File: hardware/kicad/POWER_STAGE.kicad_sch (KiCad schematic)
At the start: 0 parts

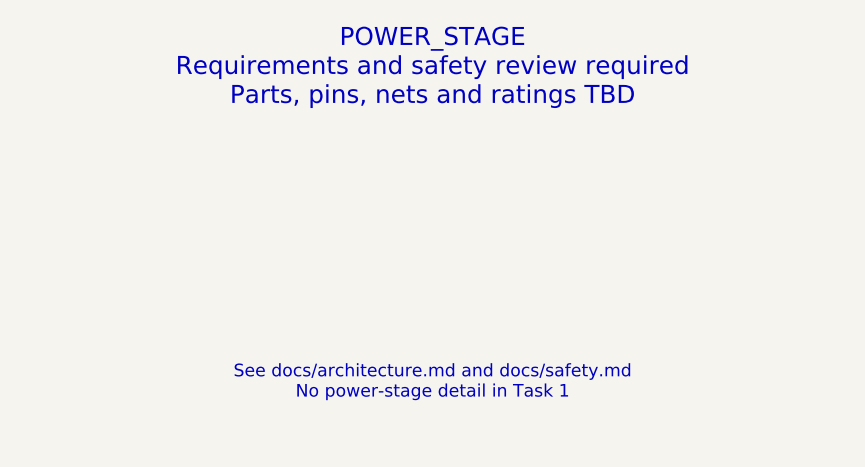
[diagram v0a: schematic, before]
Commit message: hardware: update existing KiCad architecture and add precharge sheet
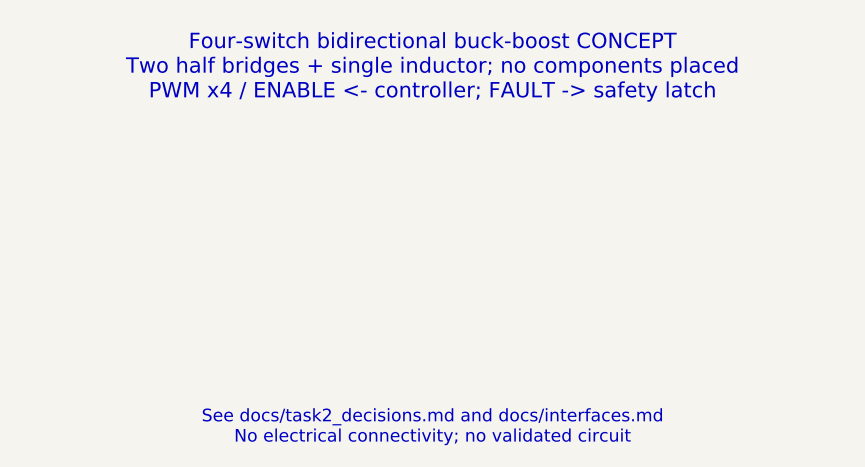
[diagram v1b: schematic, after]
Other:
- note added: "Four-switch bidirectional buck-boost CONCEPT Two half bridges + single inductor; no components placed PWM x4 / ENABLE <- controller; FAULT -> safety latch"
- note added: "See docs/task2_decisions.md and docs/interfaces.md No electrical connectivity; no validated circuit"
- note removed: "POWER_STAGE Requirements and safety review required Parts, pins, nets and ratings TBD"
- note removed: "See docs/architecture.md and docs/safety.md No power-stage detail in Task 1"
- title: POWER_STAGE - Placeholder -> POWER_STAGE - Task 2 Proposal

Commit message: hardware: implement prototype Rev A electrical schematic
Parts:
- added C1, C4: 470uF / 63V low ESR / ripple rating TBD, Capacitor_THT:CP_Radial_D12.5mm_P5.00mm, symbol RevA:C
- added C2, C3, C5, C6: 2.2uF / 100V X7R / effective C MUST VERIFY, Capacitor_SMD:C_1210_3225Metric, symbol RevA:C
- added C7, C8: 1nF /100V DNI tunable, Capacitor_SMD:C_0805_2012Metric, symbol RevA:C
- added D10, D7, D8, D9: BZT52H-C15 / gate clamp candidate, Diode_SMD:D_SOD-123F, symbol RevA:D
- added L1: XAL1510-223MED / 22uH +/-20%, Inductor_SMD:L_Coilcraft_XAL1510-223, symbol RevA:L
- added Q16, Q17, Q18, Q19: CSD18540Q5B, Package_SON:VSONP-8-1EP_5x6_P1.27mm, symbol RevA:CSD18540Q5B
- added R39, R40, R41: WSK25123L000FEA / 3mR 1% 1W, Resistor_SMD:R_Shunt_Vishay_WSK2512_6332Metric_T1.19mm, symbol RevA:WSK25123L000FEA
- added R42, R43, R44, R45: 10k GS mandatory, Resistor_SMD:R_0805_2012Metric, symbol RevA:R
- added R46, R47: 10R DNI tunable, Resistor_SMD:R_0805_2012Metric, symbol RevA:R
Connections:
- new net BUS_LINK: C1.1 (A), C2.1 (A), C3.1 (A), Q16.3 (D_DS5_6_7_8), R39.3 (K_M), R39.4 (I_M)
- new net BUS_LINK_IN: R39.1 (I_P), R39.2 (K_P)
- new net CAP_LINK: C4.1 (A), C5.1 (A), C6.1 (A), Q18.3 (D_DS5_6_7_8), R40.3 (K_M), R40.4 (I_M)
- new net CAP_LINK_IN: R40.1 (I_P), R40.2 (K_P)
- new net GATE_AH: D7.1 (K), Q16.2 (G_DS4), R42.1 (A)
- new net GATE_AL: D8.1 (K), Q17.2 (G_DS4), R43.1 (A)
- new net GATE_BH: D9.1 (K), Q18.2 (G_DS4), R44.1 (A)
- new net GATE_BL: D10.1 (K), Q19.2 (G_DS4), R45.1 (A)
- new net GND: C1.2 (B), C2.2 (B), C3.2 (B), C4.2 (B), C5.2 (B), C6.2 (B), C7.2 (B), C8.2 (B), D10.2 (A), D8.2 (A), Q17.1 (S_DS1_2_3), Q19.1 (S_DS1_2_3), R43.2 (B), R45.2 (B)
- new net IL_TO_L: L1.1 (A), R41.3 (K_M), R41.4 (I_M)
- new net SW_NODE_A: D7.2 (A), Q16.1 (S_DS1_2_3), Q17.3 (D_DS5_6_7_8), R41.1 (I_P), R41.2 (K_P), R42.2 (B), R46.1 (A)
- new net SW_NODE_A_SNUB: C7.1 (A), R46.2 (B)
- new net SW_NODE_B: D9.2 (A), L1.2 (B), Q18.1 (S_DS1_2_3), Q19.3 (D_DS5_6_7_8), R44.2 (B), R47.1 (A)
- new net SW_NODE_B_SNUB: C8.1 (A), R47.2 (B)
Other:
- note added: "Body diode S -> D: healthy all-OFF positive rails block static DC; inductor decay or a short high-side FET can feed the other rail."
- note added: "Primary fs=200kHz; normal8A/peak12A are cap average targets, not guaranteed module port peak limits."
- note added: "Shunts: power pads1/4, Kelvin pads2/3. WSK 3mR footprint terminal T=1.19mm."
- note removed: "Four-switch bidirectional buck-boost CONCEPT Two half bridges + single inductor; no components placed PWM x4 / ENABLE <- controller; FAULT -> safety latch"
- note removed: "See docs/task2_decisions.md and docs/interfaces.md No electrical connectivity; no validated circuit"
- title: POWER_STAGE - Task 2 Proposal -> POWER_STAGE / Prototype Rev A draft

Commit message: hardware: refine Rev A protection and passive selections
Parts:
- removed D10, D9: BZT52H-C15 / gate clamp candidate, Diode_SMD:D_SOD-123F, symbol RevA:D
- removed Q16, Q17, Q18, Q19: CSD18540Q5B, Package_SON:VSONP-8-1EP_5x6_P1.27mm, symbol RevA:CSD18540Q5B
- removed R42, R43, R44, R45: 10k GS mandatory, Resistor_SMD:R_0805_2012Metric, symbol RevA:R
- removed R46, R47: 10R DNI tunable, Resistor_SMD:R_0805_2012Metric, symbol RevA:R
- added C10, C11, C12, C13, C14, C9: 470uF /63V EEUFR1J471 / ripple1.995Arms at100kHz, Capacitor_THT:CP_Radial_D12.5mm_P5.00mm, symbol RevA:C
- added C15, C16: 2.2uF / 100V X7R / effective C MUST VERIFY, Capacitor_SMD:C_1210_3225Metric, symbol RevA:C
- added C17, C18: 1nF /100V DNI tunable, Capacitor_SMD:C_0805_2012Metric, symbol RevA:C
- added D5, D6: BZT52H-C15 / gate clamp candidate, Diode_SMD:D_SOD-123F, symbol RevA:D
- added Q12, Q13, Q14, Q15: CSD18540Q5B, Package_SON:VSONP-8-1EP_5x6_P1.27mm, symbol RevA:CSD18540Q5B
- added R33, R34, R35: WSK25123L000FEA / 3mR 1% 1W, Resistor_SMD:R_Shunt_Vishay_WSK2512_6332Metric_T2.21mm, symbol RevA:WSK25123L000FEA
- added R36, R37, R38: 10k GS mandatory, Resistor_SMD:R_0805_2012Metric, symbol RevA:R
- C1, C4: value 470uF / 63V low ESR / ripple rating TBD -> 470uF /63V EEUFR1J471 / ripple1.995Arms at100kHz; MPN (none) -> EEUFR1J471
- C2, C3, C5, C6: value 2.2uF / 100V X7R / effective C MUST VERIFY -> 470uF /63V EEUFR1J471 / ripple1.995Arms at100kHz; footprint Capacitor_SMD:C_1210_3225Metric -> Capacitor_THT:CP_Radial_D12.5mm_P5.00mm; MPN (none) -> EEUFR1J471
- C7, C8: value 1nF /100V DNI tunable -> 2.2uF / 100V X7R / effective C MUST VERIFY; footprint Capacitor_SMD:C_0805_2012Metric -> Capacitor_SMD:C_1210_3225Metric; MPN (none) -> GRM32ER72A225KA35L; now fitted
- D7, D8: MPN (none) -> BZT52H-C15
- L1: MPN (none) -> XAL1510-223MED
- R39: value WSK25123L000FEA / 3mR 1% 1W -> 10k GS mandatory; footprint Resistor_SMD:R_Shunt_Vishay_WSK2512_6332Metric_T1.19mm -> Resistor_SMD:R_0805_2012Metric; symbol RevA:WSK25123L000FEA -> RevA:R; MPN (none) -> CRCW080510K0FKEA
- R40, R41: value WSK25123L000FEA / 3mR 1% 1W -> 10R DNI tunable; footprint Resistor_SMD:R_Shunt_Vishay_WSK2512_6332Metric_T1.19mm -> Resistor_SMD:R_0805_2012Metric; symbol RevA:WSK25123L000FEA -> RevA:R; MPN (none) -> CRCW080510R0FKEA; now not fitted
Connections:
- net BUS_LINK: now also C4.1 (A), C5.1 (A), C6.1 (A), C7.1 (A), C8.1 (A), Q12.3 (D_DS5_6_7_8), R33.3 (K_M), R33.4 (I_M); no longer R39.3 (K_M), R39.4 (I_M)
- net BUS_LINK_IN: now also R33.1 (I_P), R33.2 (K_P); no longer R39.1 (I_P), R39.2 (K_P)
- net CAP_LINK: now also C10.1 (A), C11.1 (A), C12.1 (A), C13.1 (A), C14.1 (A), C15.1 (A), C16.1 (A), C9.1 (A), Q14.3 (D_DS5_6_7_8), R34.3 (K_M), R34.4 (I_M); no longer C4.1 (A), C5.1 (A), C6.1 (A), R40.3 (K_M), R40.4 (I_M)
- net CAP_LINK_IN: now also R34.1 (I_P), R34.2 (K_P); no longer R40.1 (I_P), R40.2 (K_P)
- net GATE_AH: now also D5.1 (K), Q12.2 (G_DS4), R36.1 (A); no longer D7.1 (K)
- net GATE_AL: now also D6.1 (K), Q13.2 (G_DS4), R37.1 (A); no longer D8.1 (K)
- net GATE_BH: now also D7.1 (K), Q14.2 (G_DS4), R38.1 (A)
- net GATE_BL: now also D8.1 (K), R39.1 (A), Q15.2 (G_DS4)
- net GND: now also R39.2 (B), C10.2 (B), C11.2 (B), C12.2 (B), C13.2 (B), C14.2 (B), C15.2 (B), C16.2 (B), C17.2 (B), C18.2 (B), C9.2 (B), D6.2 (A), Q13.1 (S_DS1_2_3), Q15.1 (S_DS1_2_3), R37.2 (B)
- net IL_TO_L: now also R35.3 (K_M), R35.4 (I_M); no longer R41.3 (K_M), R41.4 (I_M)
- net SW_NODE_A: now also R40.1 (A), D5.2 (A), Q12.1 (S_DS1_2_3), Q13.3 (D_DS5_6_7_8), R35.1 (I_P), R35.2 (K_P), R36.2 (B); no longer D7.2 (A), R41.1 (I_P), R41.2 (K_P)
- net SW_NODE_A_SNUB: now also R40.2 (B), C17.1 (A); no longer C7.1 (A)
- net SW_NODE_B: now also D7.2 (A), R41.1 (A), Q14.1 (S_DS1_2_3), Q15.3 (D_DS5_6_7_8), R38.2 (B)
- net SW_NODE_B_SNUB: now also R41.2 (B), C18.1 (A); no longer C8.1 (A)
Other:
- note added: "Primary fs=200kHz; initial average current cap9.5A maximum,8A normal;12A remains later design goal."
- note added: "Shunts: power pads1/4, Kelvin pads2/3. WSK3mR terminal T=2.21mm (not the>=5mR T1.19 land)."
- note removed: "Primary fs=200kHz; normal8A/peak12A are cap average targets, not guaranteed module port peak limits."
- note removed: "Shunts: power pads1/4, Kelvin pads2/3. WSK 3mR footprint terminal T=1.19mm."
- moved on the sheet: D7, D8, L1

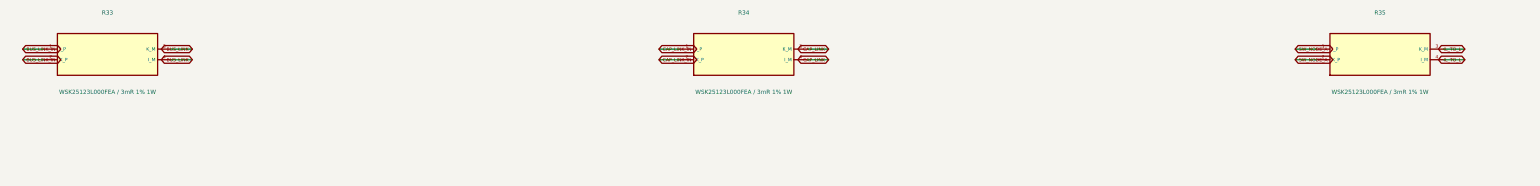
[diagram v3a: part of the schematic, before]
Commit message: hardware: define PCB harness boundary and Kelvin nets
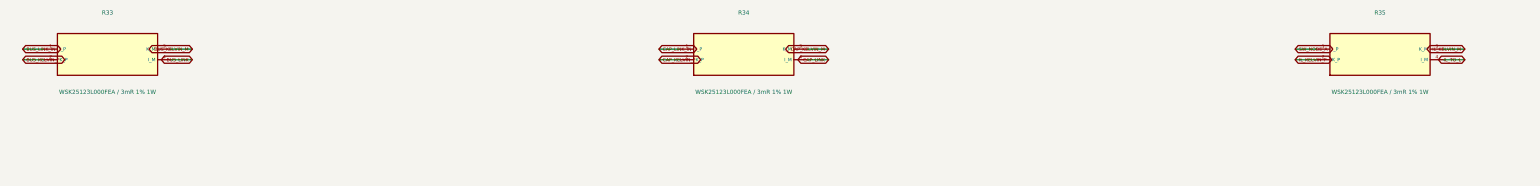
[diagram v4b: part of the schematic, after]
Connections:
- net BUS_LINK: no longer R33.3 (K_M)
- net BUS_LINK_IN: no longer R33.2 (K_P)
- net CAP_LINK: no longer R34.3 (K_M)
- net CAP_LINK_IN: no longer R34.2 (K_P)
- net IL_TO_L: no longer R35.3 (K_M)
- net SW_NODE_A: no longer R35.2 (K_P)
- new net BUS_KELVIN_M: R33.3 (K_M)
- new net BUS_KELVIN_P: R33.2 (K_P)
- new net CAP_KELVIN_M: R34.3 (K_M)
- new net CAP_KELVIN_P: R34.2 (K_P)
- new net IL_KELVIN_M: R35.3 (K_M)
- new net IL_KELVIN_P: R35.2 (K_P)
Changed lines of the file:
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@@
   (generator "eeschema")
   (paper "User" 1189 841)
-  (title_block (title "POWER_STAGE / Prototype Rev A draft") (rev "RevA-draft") (comment 1 "ASSUMPTION - MUST VERIFY ON PROTOTYPE; no PCB placement"))
+  (title_block (title "POWER_STAGE / Prototype Rev A draft") (rev "RevA-draft") (comment 1 "ASSUMPTION - MUST VERIFY ON PROTOTYPE; PCB engineering authorized"))
   (symbol
     (lib_id "RevA:WSK25123L000FEA")
@@
   )
   (wire (pts (xy 73.66 115.57) (xy 68.58 115.57)) (stroke (width 0) (type default)))
-  (global_label "BUS_LINK_IN"
+  (global_label "BUS_KELVIN_P"
     (shape bidirectional)
     (at 68.58 115.57 0)
@@
   )
   (wire (pts (xy 104.14 113.03) (xy 109.22 113.03)) (stroke (width 0) (type default)))
-  (global_label "BUS_LINK"
+  (global_label "BUS_KELVIN_M"
     (shape bidirectional)
     (at 109.22 113.03 180)
@@
   )
   (wire (pts (xy 226.06 115.57) (xy 220.98 115.57)) (stroke (width 0) (type default)))
-  (global_label "CAP_LINK_IN"
+  (global_label "CAP_KELVIN_P"
     (shape bidirectional)
     (at 220.98 115.57 0)
@@
   )
   (wire (pts (xy 256.54 113.03) (xy 261.62 113.03)) (stroke (width 0) (type default)))
-  (global_label "CAP_LINK"
+  (global_label "CAP_KELVIN_M"
     (shape bidirectional)
     (at 261.62 113.03 180)
@@
   )
   (wire (pts (xy 378.46 115.57) (xy 373.38 115.57)) (stroke (width 0) (type default)))
-  (global_label "SW_NODE_A"
+  (global_label "IL_KELVIN_P"
     (shape bidirectional)
     (at 373.38 115.57 0)
@@
   )
   (wire (pts (xy 408.94 113.03) (xy 414.02 113.03)) (stroke (width 0) (type default)))
-  (global_label "IL_TO_L"
+  (global_label "IL_KELVIN_M"
     (shape bidirectional)
     (at 414.02 113.03 180)
